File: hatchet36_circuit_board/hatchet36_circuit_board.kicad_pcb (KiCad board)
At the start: 2 copper layers, 288 x 204 mm, 82 parts, among them J1 Conn_01x04_Female, SW1 SW_Push, SW10 SW_Push, SW11 SW_Push, SW12 SW_Push, SW13 SW_Push, SW14 SW_Push, SW15 SW_Push, SW16 SW_Push, SW17 SW_Push, SW18 SW_Push, SW19 SW_Push, SW2 SW_Push, SW20 SW_Push, SW21 SW_Push, SW22 SW_Push, SW23 SW_Push, SW24 SW_Push, SW25 SW_Push, SW26 SW_Push, SW27 SW_Push, SW28 SW_Push, SW29 SW_Push, SW3 SW_Push, SW30 SW_Push, SW31 SW_Push, SW32 SW_Push, SW33 SW_Push, SW34 SW_Push, SW35 SW_Push, SW36 SW_Push, SW37 SW_Push, SW38 SW_SPDT, SW4 SW_Push, SW5 SW_Push, SW6 SW_Push, SW7 SW_Push, SW8 SW_Push, SW9 SW_Push, U1 BL652

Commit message: align diode
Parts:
- BT1, BT2: moved to B.Cu
- moved BT2 170.0 mm to (206.0, 109.5), turned to 180 degrees
- moved D19 142.3 mm to (203.0, 70.5)
- moved D17 138.0 mm to (167.0, 70.5)
- moved D9 137.0 mm to (203.0, 53.5)
- moved D20 133.3 mm to (221.0, 70.5)
- moved D29 130.8 mm to (203.0, 87.5)
- moved D30 123.3 mm to (221.0, 87.5)
- moved D36 118.0 mm to (185.0, 104.5)
- moved D38 114.8 mm to (51.5, 127.0), turned to 180 degrees
- moved C2 114.8 mm to (74.0, 104.5), turned to 180 degrees
- moved D5 113.4 mm to (131.0, 53.5)
- moved D27 109.9 mm to (167.0, 87.5)
- moved D37 103.9 mm to (61.0, 142.2), turned to 180 degrees
- moved D14 103.5 mm to (113.0, 70.5)
- moved D18 96.7 mm to (185.0, 70.5)
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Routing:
- net /row1: track 0.00 -> 168.9 mm
- net /row2: track 0.00 -> 168.9 mm
- net /row0: track 18.9 -> 169.0 mm
- net /row3: track 0.00 -> 93.8 mm
- net /col7: track 0.00 -> 56.2 mm
- net /col6: track 0.00 -> 56.2 mm
- net /col5: track 0.00 -> 56.2 mm
- net /col4: track 0.00 -> 56.2 mm
- net /col3: track 0.00 -> 56.2 mm
- net /col2: track 0.00 -> 56.2 mm
- net /col1: track 0.00 -> 37.4 mm
- net /col9: track 0.00 -> 37.4 mm
- net /col8: track 0.00 -> 37.4 mm
- net /col0: track 0.00 -> 37.4 mm
- net Net-(D33-Pad2): track 0.00 -> 14.4 mm
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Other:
- board outline removed

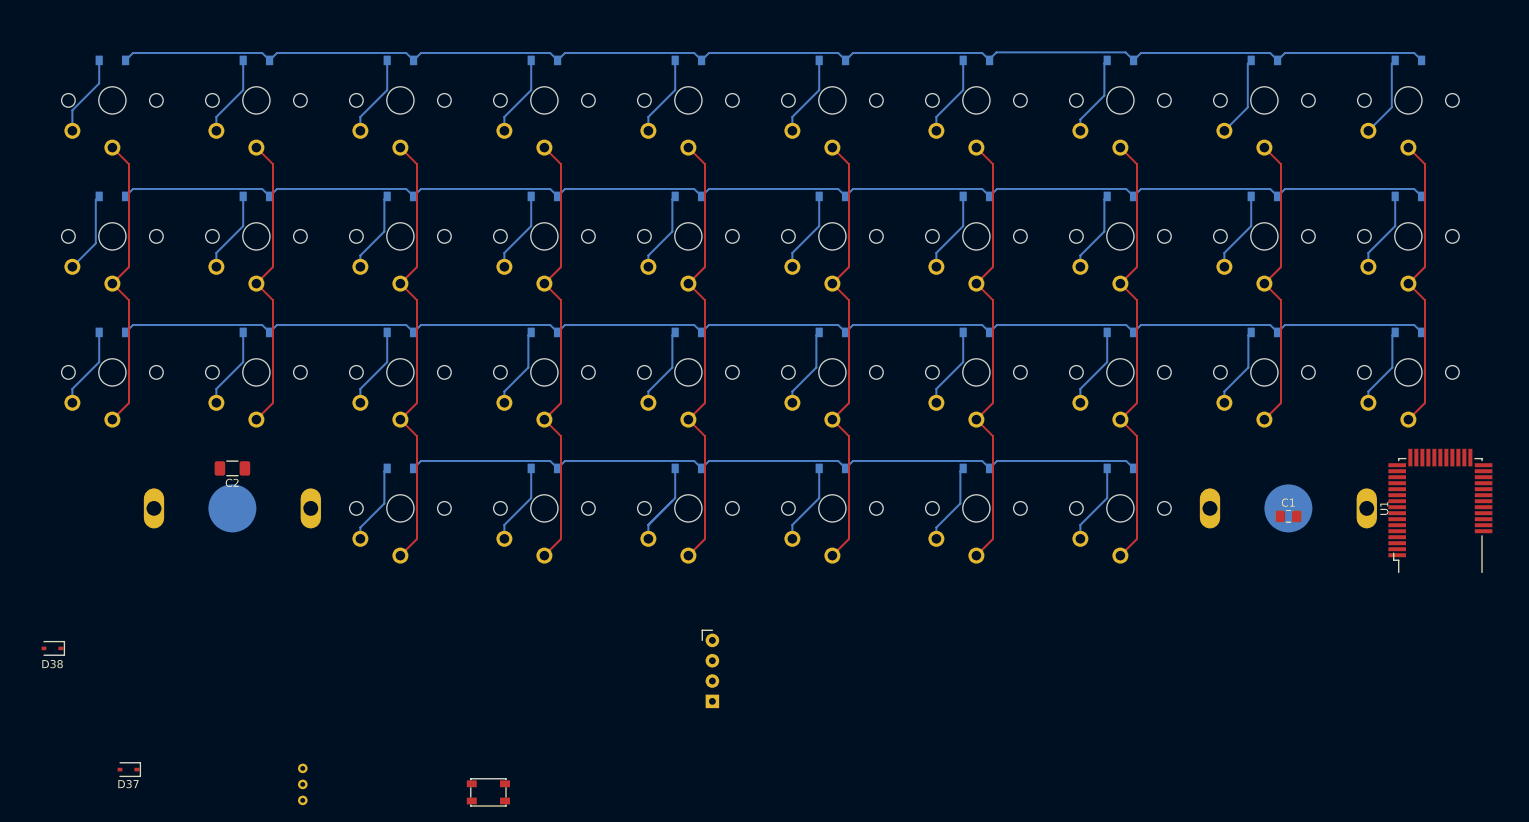
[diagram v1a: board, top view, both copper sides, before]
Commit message: add connector
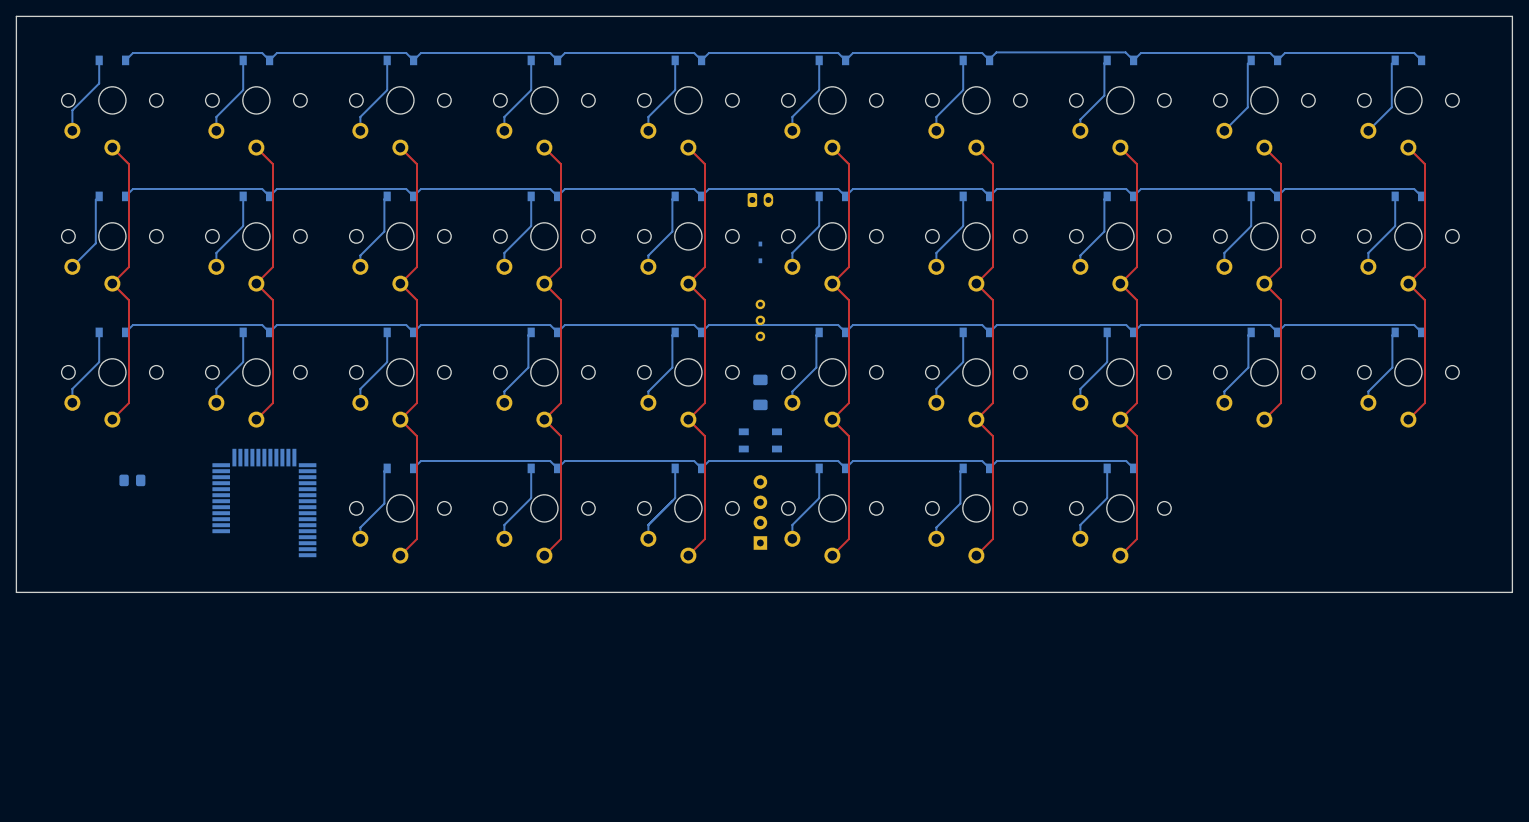
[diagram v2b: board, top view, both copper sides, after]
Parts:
- removed BT1, BT2: Battery_Cell, locallib:CR1632-case
- removed D38: D_Schottky, Diode_SMD:D_SOD-323
- added J2: Conn_01x04_Female, locallib:programming_port, B.Cu at (140.0, 106.2)
- C1, C2, D37, SW37, U1: moved to B.Cu
- J1: value Conn_01x04_Female -> Conn_01x02_Female; footprint locallib:programming_port -> Connector_JST:JST_PH_S2B-PH-K_1x02_P2.00mm_Horizontal; moved to B.Cu
- moved U1 147.0 mm to (78.0, 109.5)
- moved C1 144.6 mm to (61.5, 106.0), turned to 180 degrees
- moved D37 102.1 mm to (140.0, 77.5), turned to 90 degrees
- moved SW38 81.5 mm to (140.0, 84.0)
- moved C2 66.7 mm to (140.0, 95.0), turned to -90 degrees
- moved SW37 55.6 mm to (140.0, 101.0), turned to 180 degrees
- moved J1 55.3 mm to (139.0, 71.0)
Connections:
- D37 pad 2: Net-(BT1-Pad1) -> Net-(D37-Pad2)
- J1 pad 1: /SWDCLK -> Net-(D37-Pad2)
- J1 pad 2: /SWDIO -> GND
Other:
- board outline added: 187 x 72 mm

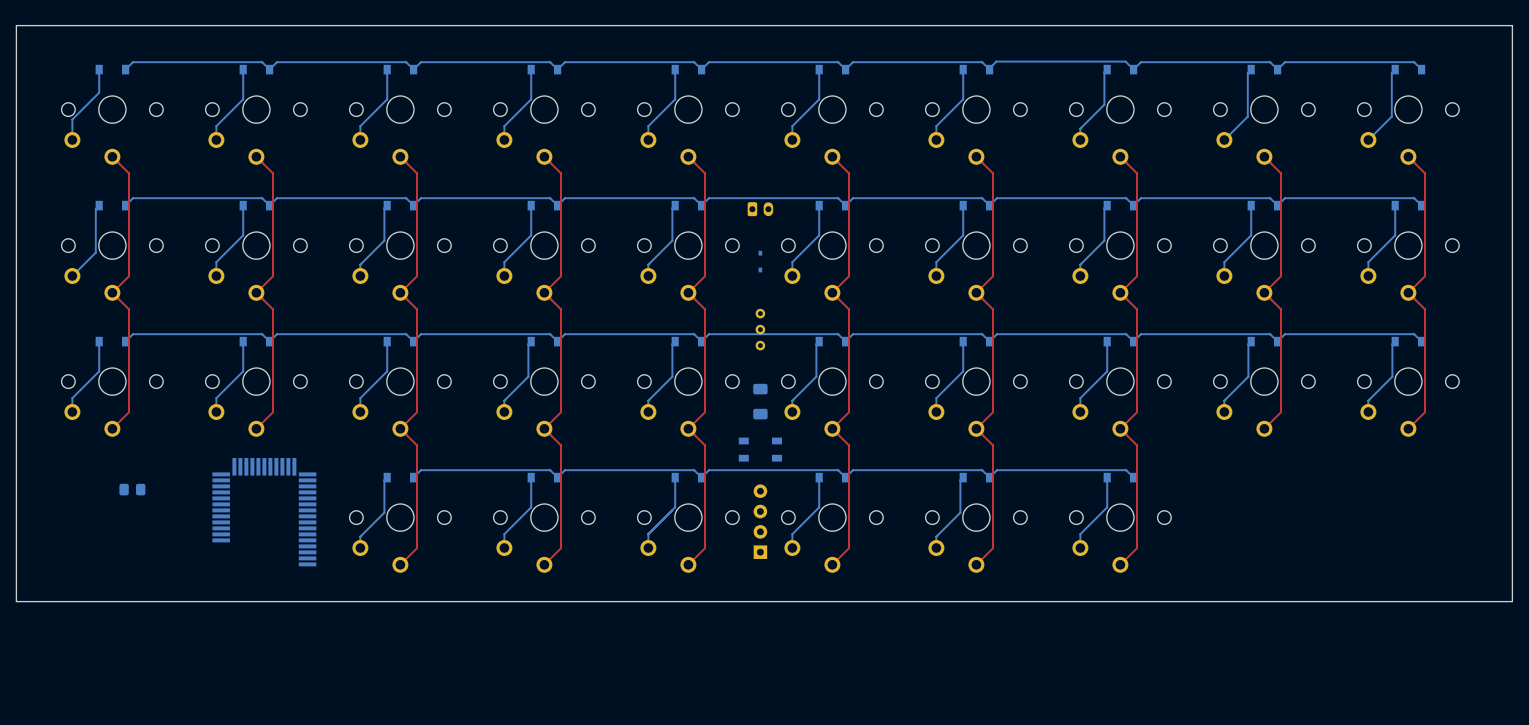
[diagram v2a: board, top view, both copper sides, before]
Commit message: mod for two battery
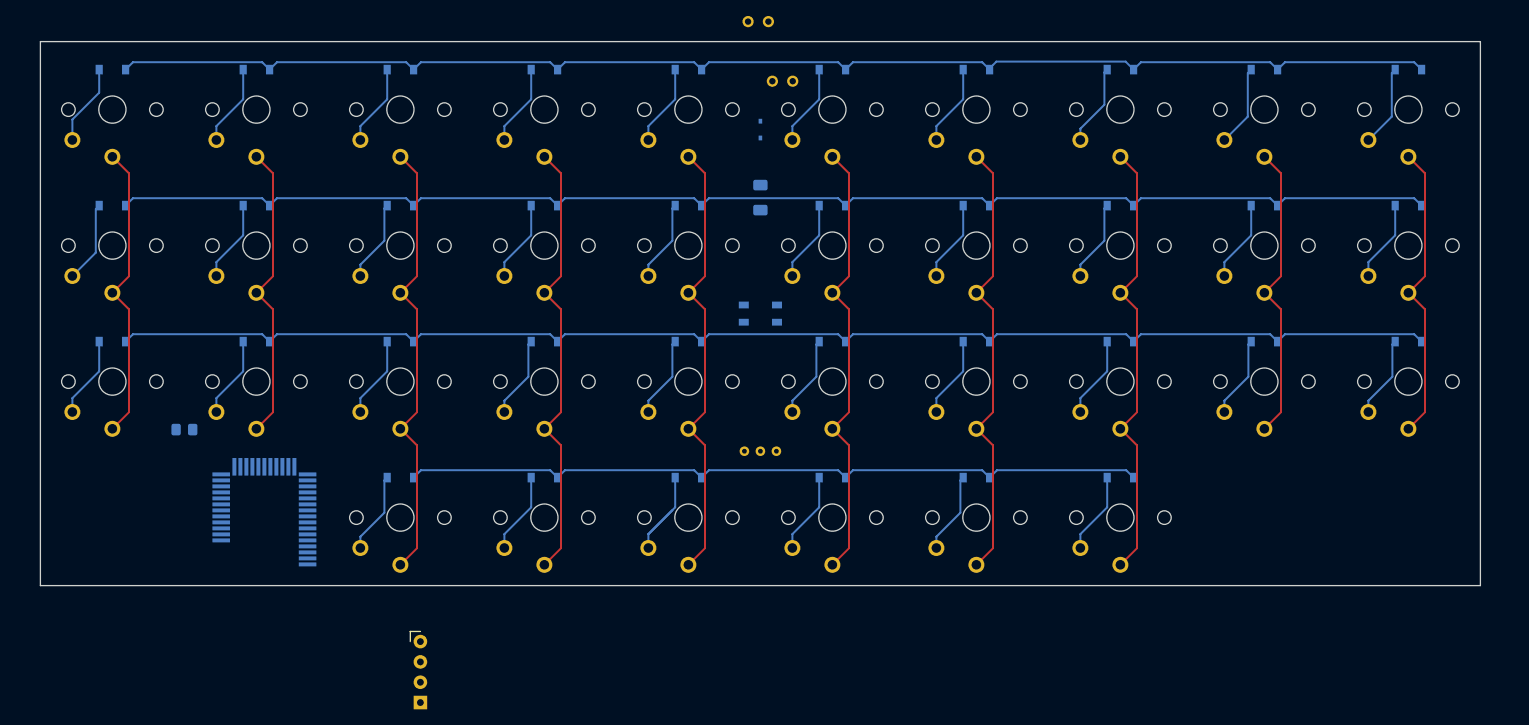
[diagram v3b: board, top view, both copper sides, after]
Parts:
- added J3: Conn_01x04_Female, locallib:programming_port, F.Cu at (97.5, 125.0)
- J1: footprint Connector_JST:JST_PH_S2B-PH-K_1x02_P2.00mm_Horizontal -> TestPoint:TestPoint_2Pads_Pitch2.54mm_Drill0.8mm
- J2: value Conn_01x04_Female -> Conn_01x02_Female; footprint locallib:programming_port -> TestPoint:TestPoint_2Pads_Pitch2.54mm_Drill0.8mm
- moved J2 51.3 mm to (141.5, 55.0), turned to 0 degrees
- moved C2 25.5 mm to (140.0, 69.5)
- moved J1 23.5 mm to (138.5, 47.5)
- moved SW38 17.3 mm to (138.0, 101.2), turned to 90 degrees
- moved SW37 17.0 mm to (140.0, 84.0)
- moved D37 16.5 mm to (140.0, 61.0)
- moved C1 9.92 mm to (68.0, 98.5)
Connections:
- J1 pad 2: GND -> Net-(J1-Pad2)
- J2 pad 1: /SWDCLK -> Net-(J1-Pad2)
- J2 pad 2: /SWDIO -> GND
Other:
- board size 187 x 72 mm -> 180 x 68 mm

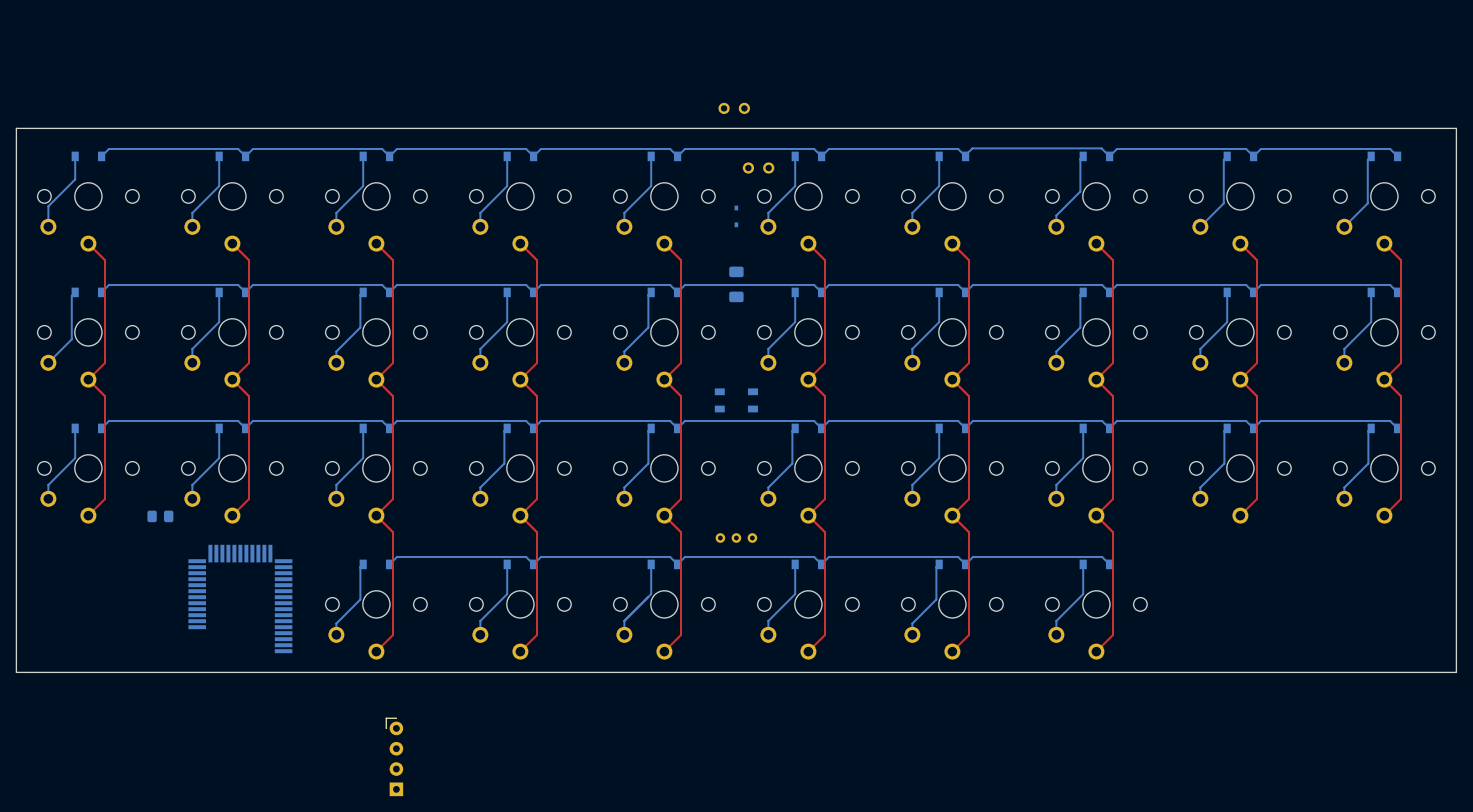
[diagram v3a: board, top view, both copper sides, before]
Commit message: put all parts on pcb
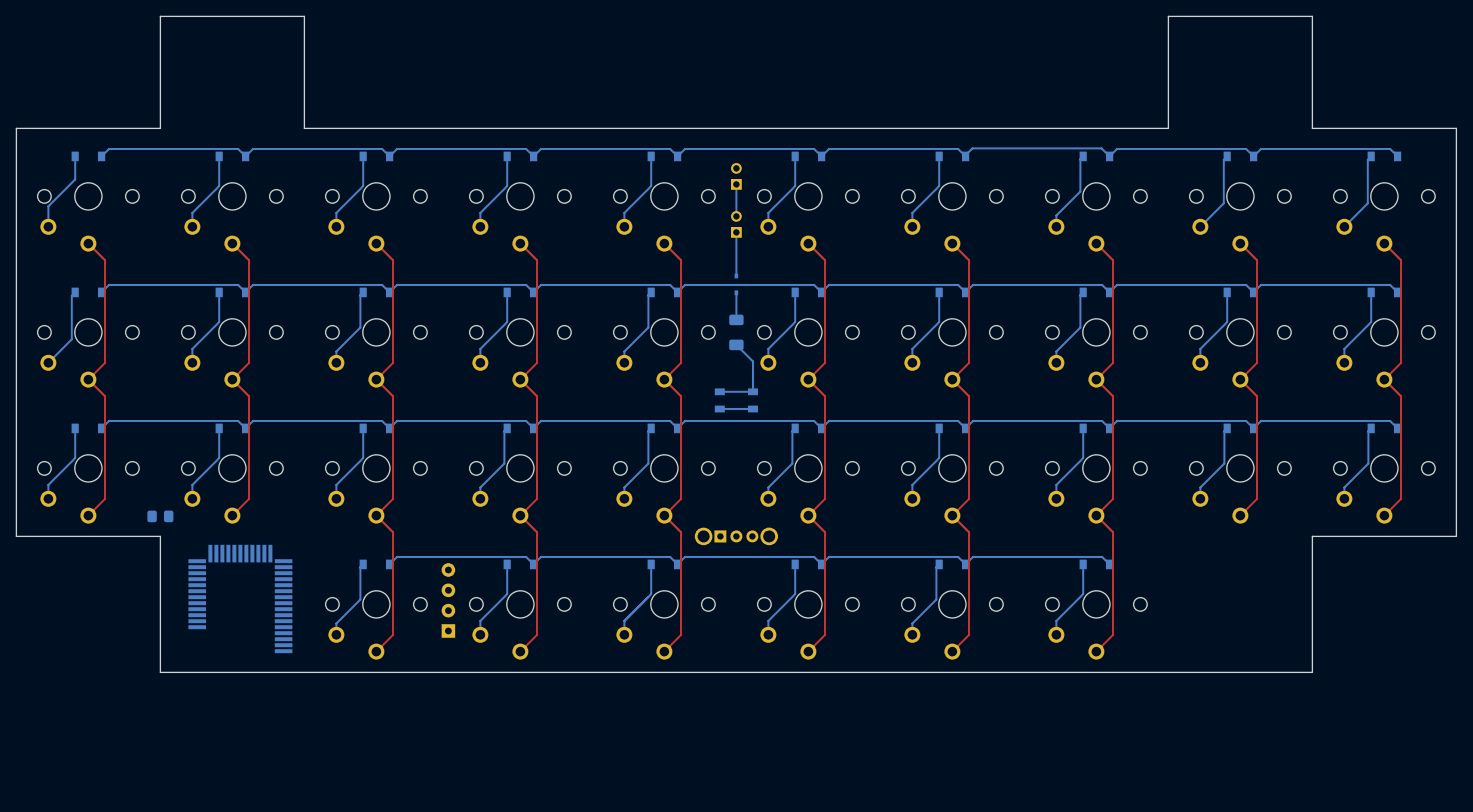
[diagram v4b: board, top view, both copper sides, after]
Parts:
- J1, J2: footprint TestPoint:TestPoint_2Pads_Pitch2.54mm_Drill0.8mm -> Connector_PinHeader_2.00mm:PinHeader_1x02_P2.00mm_Vertical
- J3: moved to B.Cu
- SW38: footprint locallib:slide_switch_vertical_01x03_pitch2mm -> locallib:SW_Slide_1P2T_CK_OS102011MS2Q_SmallPad; moved to B.Cu
- moved J3 20.8 mm to (104.0, 105.2), turned to 180 degrees
- moved J1 15.6 mm to (140.0, 63.0)
- moved D37 8.50 mm to (140.0, 69.5)
- moved C2 6.00 mm to (140.0, 75.5)
- moved J2 2.54 mm to (140.0, 57.0)
- moved SW38 0.20 mm to (138.0, 101.0), turned to 0 degrees
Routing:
- net GND: track 0.00 -> 10.9 mm
- net Net-(D37-Pad2): track 0.00 -> 5.45 mm
- net Net-(SW37-Pad2): track 0.00 -> 4.15 mm
- net Net-(J1-Pad2): track 0.00 -> 4.00 mm
- net Net-(C2-Pad1): track 0.00 -> 3.39 mm
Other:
- board size 180 x 68 mm -> 180 x 82 mm

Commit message: made pcb which can work
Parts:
- moved J3 8.20 mm to (104.0, 113.4), turned to 0 degrees
- moved C1 5.52 mm to (73.5, 99.0), turned to 0 degrees
- moved SW38 4.00 mm to (142.0, 101.0), turned to 180 degrees
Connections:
- U1 pad 10: /col7 -> unconnected-(U1-Pad10)
- U1 pad 11: /col5 -> /col7
- U1 pad 12: /col2 -> unconnected-(U1-Pad12)
- U1 pad 13: /col1 -> /col6
- U1 pad 14: /col0 -> unconnected-(U1-Pad14)
- U1 pad 15: unconnected-(U1-Pad15) -> /col5
- U1 pad 17: /row2 -> /col4
- U1 pad 18: /row1 -> /col3
- U1 pad 19: /row0 -> unconnected-(U1-Pad19)
- U1 pad 20: unconnected-(U1-Pad20) -> /col2
- U1 pad 22: unconnected-(U1-Pad22) -> /col1
- U1 pad 28: /col4 -> /row2
- U1 pad 29: /col6 -> unconnected-(U1-Pad29)
- U1 pad 30: /col8 -> /col0
- U1 pad 32: unconnected-(U1-Pad32) -> /row1
- U1 pad 34: unconnected-(U1-Pad34) -> /row0
- U1 pad 36: /col9 -> unconnected-(U1-Pad36)
- U1 pad 37: /col3 -> unconnected-(U1-Pad37)
- U1 pad 7: unconnected-(U1-Pad7) -> /col9
- U1 pad 9: unconnected-(U1-Pad9) -> /col8
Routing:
- net GND: track 10.9 -> 177.9 mm, vias 0 -> 7
- net /col9: track 37.4 -> 180.2 mm
- net /col8: track 37.4 -> 161.6 mm
- net /col7: track 56.2 -> 162.7 mm
- net VDD: track 0.00 -> 102.5 mm, vias 0 -> 1
- net /col6: track 56.2 -> 144.1 mm
- net Net-(SW37-Pad2): track 4.15 -> 79.4 mm, vias 0 -> 2
- net /row0: track 169.0 -> 242.4 mm
- net /col5: track 56.2 -> 124.4 mm
- net /row1: track 168.9 -> 223.9 mm
- net /col4: track 56.2 -> 107.4 mm
- net /col3: track 56.2 -> 90.9 mm
- net Net-(C2-Pad1): track 3.39 -> 32.1 mm, vias 0 -> 1
- net /SWDCLK: track 0.00 -> 25.5 mm
- net /SWDIO: track 0.00 -> 24.4 mm
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- added copper zone on B.Cu, net GND
- added copper zone on F.Cu, net GND
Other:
- outline, holes or cut-outs redrawn
- board text added: "GND"
- board text added: "OFF"
- board text added: "ON"
- board text added: "VDD"
- board text added: "hatchet36lp v1 by ak1_"
